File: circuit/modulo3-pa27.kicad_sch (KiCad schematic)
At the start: 48 parts, among them J1 CONN_01X02, J3 CONN_01X04, J4 JACK_MONO, J5 HOLE, J7 HOLE, SW1 bright, U1 OPA2134, U2 OPA2134, U3 TLE2426, U4 PWR_CONN

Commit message: ready to panelize
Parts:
- removed J1: CONN_01X02, myAmp:PIN_1x02, symbol myAmp:CONN_01X02
- removed J3: CONN_01X04, myAmp:PIN_1x04, symbol myAmp:CONN_01X04
- removed J4: JACK_MONO, myAmp:JACK_CL13106, symbol myAmp:JACK_MONO
- removed J5, J7: HOLE, myAmp:MountingHole, symbol myAmp:HOLE
- removed U4: PWR_CONN, myAmp:PWR_CONN, symbol myAmp:PWR_CONN
- added U4: ~, myAmp:EXT_JACK, symbol myAmp:EXT_JACK
- added U5: ~, myAmp:PREAMP_CONN, symbol myAmp:PREAMP_CONN
- C22, C23, C9: footprint myAmp:C_5MM_1206 -> myAmp:C_1206
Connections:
- net GND: now also U4.1 (SLEEVE)
- net PA_OUT: now also U5.5 (LEFT), U5.6 (RIGHT)
- net at R1.2: now also U4.2 (TIP)
- net +24V renamed +28V
- net +28V: now also U5.4 (30V)
- no-connect marks 3 -> 2
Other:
- moved on the sheet: C24

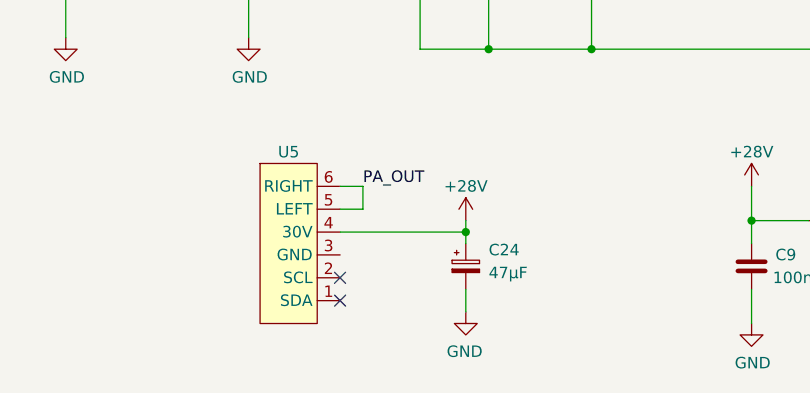
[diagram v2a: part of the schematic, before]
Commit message: fixed blunder in pa27; added stubs for some of the source files
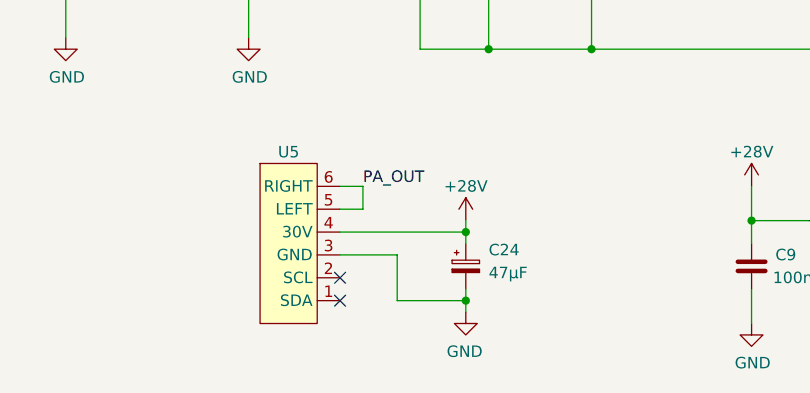
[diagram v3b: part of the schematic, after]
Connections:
- net GND: now also U5.3 (GND)
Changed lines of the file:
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@@
   (junction (at 152.4 83.82) (diameter 0) (color 0 0 0 0)
+  )
+  (junction (at 68.58 111.76) (diameter 0) (color 0 0 0 0)
   )
   (junction (at 68.58 104.14) (diameter 0) (color 0 0 0 0)
@@
     (stroke (width 0) (type default))
   )
+  (wire (pts (xy 60.96 106.68) (xy 60.96 111.76))
+    (stroke (width 0) (type default))
+  )
   (wire (pts (xy 144.78 41.91) (xy 144.78 54.61))
     (stroke (width 0) (type default))
@@
     (stroke (width 0) (type default))
   )
+  (wire (pts (xy 68.58 111.76) (xy 68.58 113.03))
+    (stroke (width 0) (type default))
+  )
   (wire (pts (xy 232.41 67.31) (xy 232.41 83.82))
     (stroke (width 0) (type default))
@@
     (stroke (width 0) (type default))
   )
-  (wire (pts (xy 68.58 110.49) (xy 68.58 113.03))
+  (wire (pts (xy 68.58 110.49) (xy 68.58 111.76))
     (stroke (width 0) (type default))
   )
@@
     (stroke (width 0) (type default))
   )
+  (wire (pts (xy 60.96 111.76) (xy 68.58 111.76))
+    (stroke (width 0) (type default))
+  )
   (wire (pts (xy 227.33 36.83) (xy 233.68 36.83))
     (stroke (width 0) (type default))
@@
     (stroke (width 0) (type default))
   )
+  (wire (pts (xy 54.61 106.68) (xy 60.96 106.68))
+    (stroke (width 0) (type default))
+  )
